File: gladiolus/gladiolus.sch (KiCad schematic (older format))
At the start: 143 parts, among them J1 NEIGHBOR1, J2 NEIGHBOR2, J7 BONUS_ROW, Q1 Q_NPN_BEC, U1 THS4520RGT, U2 AD8330ARQZ, U3 AD9283, U4 AD9704, U5 LMH6643, U6 74LVC1G3157, U7 74LVC1G3157

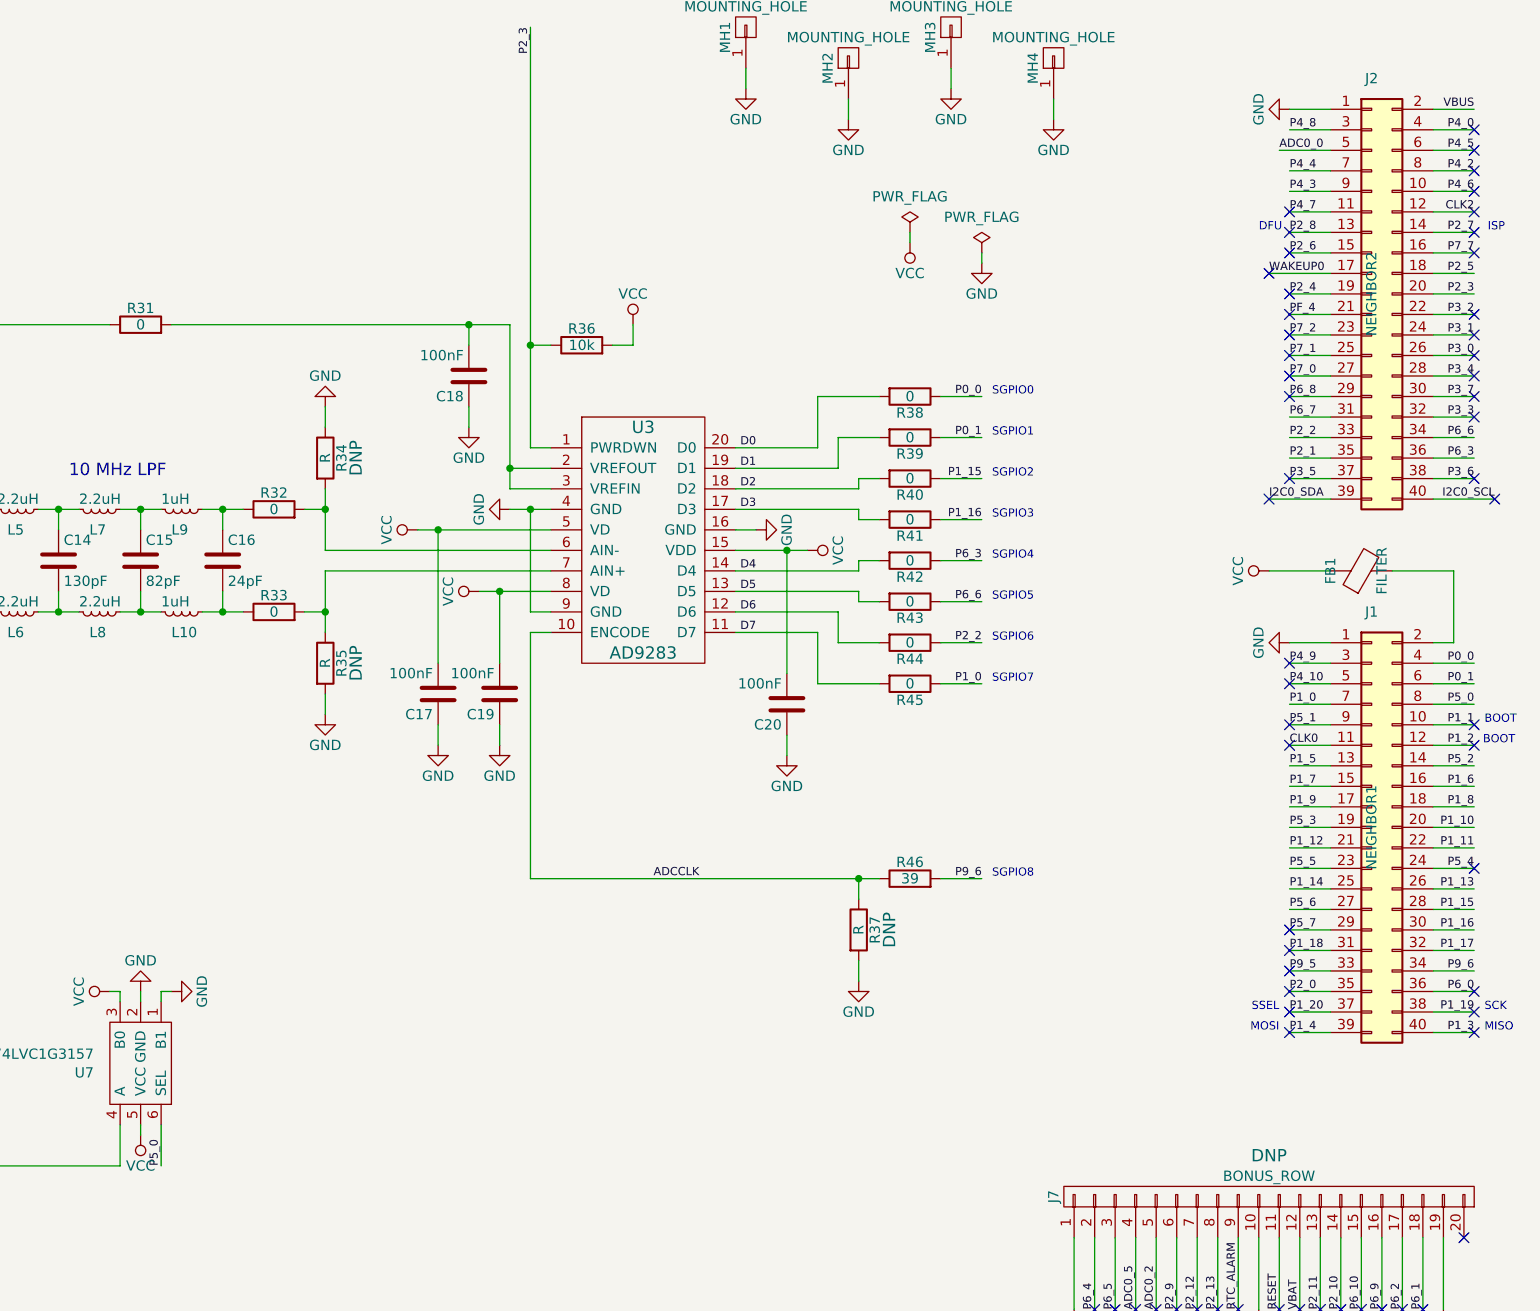
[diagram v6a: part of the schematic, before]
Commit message: Changed TX switch control to J1_24 and the ADC clock to J2_P6
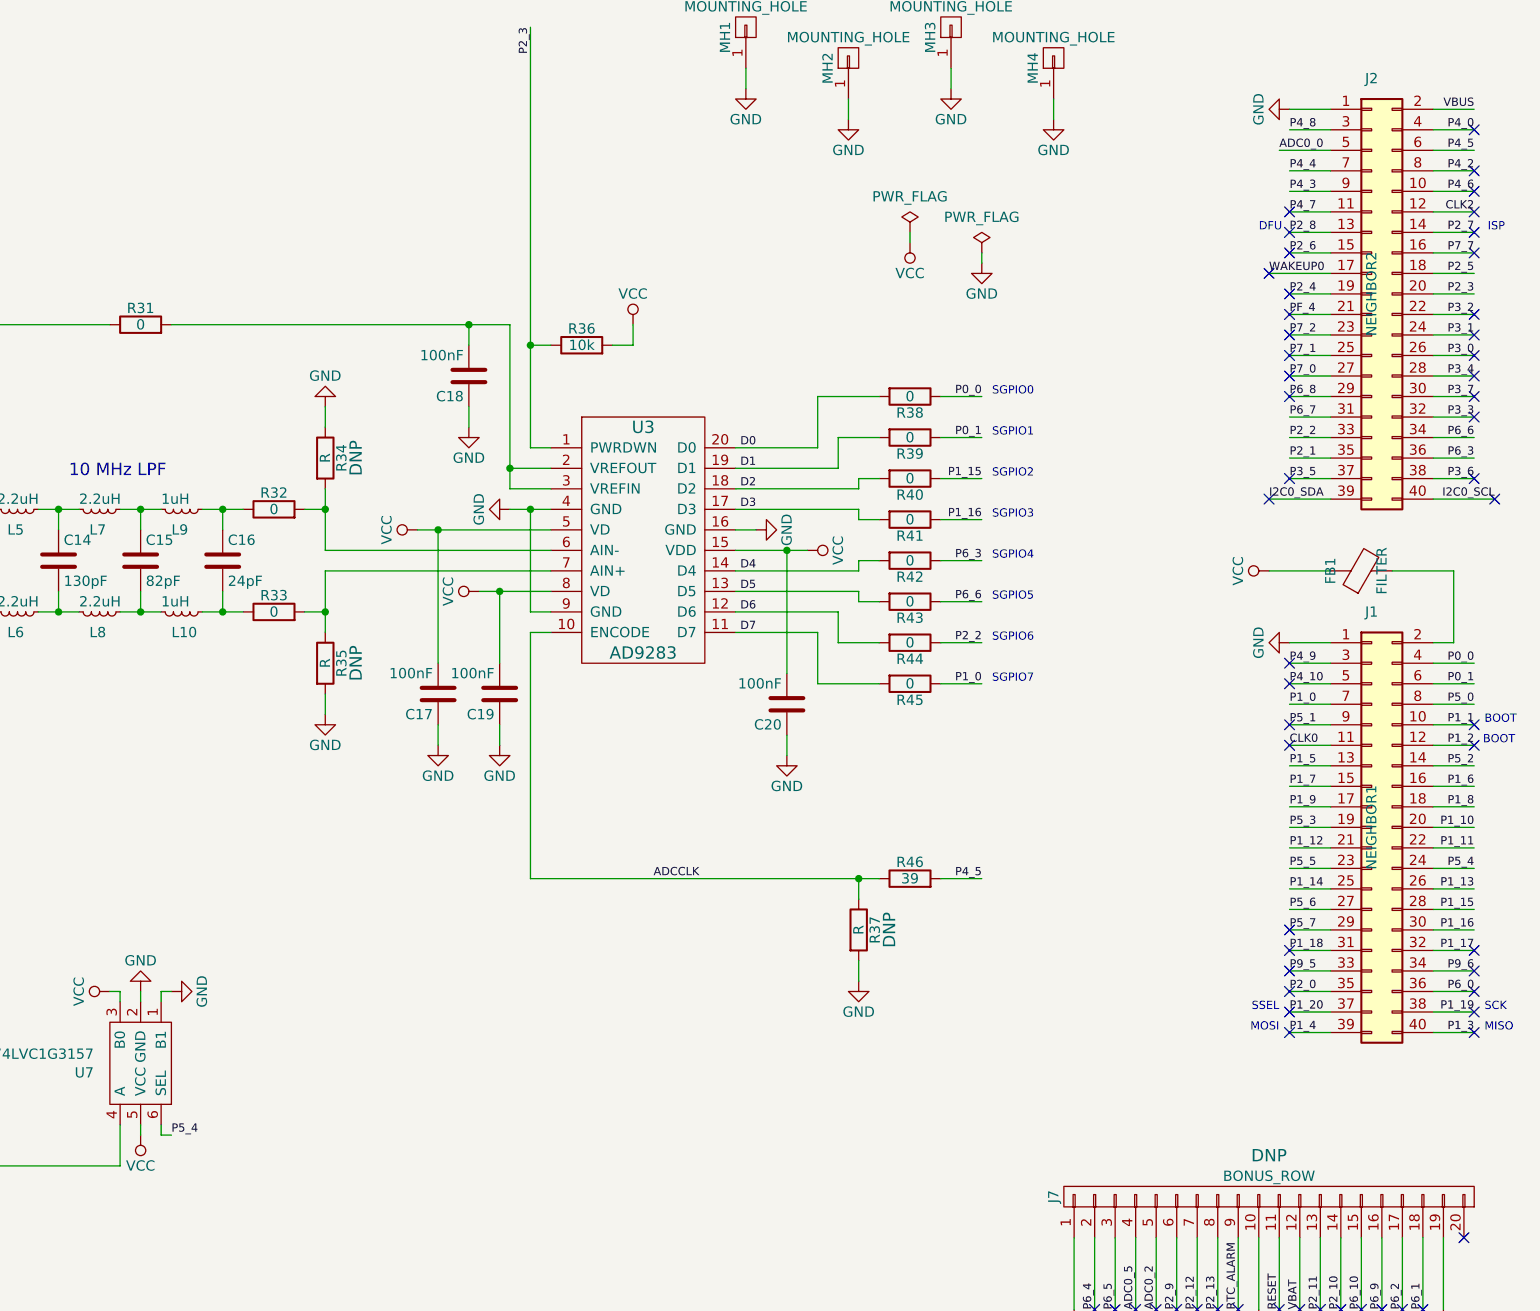
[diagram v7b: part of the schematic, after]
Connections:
- net P4_5: now also R46.2
- net P5_0: no longer U7.6 (SEL)
- net P5_4: now also U7.6 (SEL)
- net P9_6: no longer R46.2
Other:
- note removed: "SGPIO8"
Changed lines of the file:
@@
 	1    0    0    -1
 $EndComp
-Text Label 13800 4950 2    40   ~ 0
-P9_6
-Text Notes 13850 4950 0    40   ~ 0
-SGPIO8
 Text Label 6850 800  3    40   ~ 0
 ADC0_0
@@
 NoConn ~ 16200 2500
 NoConn ~ 16200 2400
-NoConn ~ 16200 2300
 NoConn ~ 16200 2200
 NoConn ~ 16200 1900
@@
 NoConn ~ 16200 1600
 NoConn ~ 16200 1500
-NoConn ~ 16200 1400
 NoConn ~ 16200 1300
 NoConn ~ 15300 3900
@@
 NoConn ~ 16200 5600
 NoConn ~ 16200 5500
-NoConn ~ 16200 4900
 NoConn ~ 16200 4200
 NoConn ~ 16200 4300
@@
 Wire Wire Line
 	9700 5500 9700 5550
-Text Label 9800 6350 1    40   ~ 0
-P5_0
-Wire Wire Line
-	9800 6150 9800 6350
 Wire Wire Line
 	4150 6900 5150 6900
@@
 Wire Wire Line
 	4800 7500 5050 7500
+Wire Wire Line
+	9800 6200 9800 6150
+Wire Wire Line
+	9800 6200 9850 6200
+NoConn ~ 16200 2300
+Text Label 9850 6200 0    40   ~ 0
+P5_4
+Text Label 13800 4950 2    40   ~ 0
+P4_5
+NoConn ~ 16200 5300
+NoConn ~ 16200 5400
 $EndSCHEMATC
